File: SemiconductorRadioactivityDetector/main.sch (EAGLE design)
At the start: 27 parts, among them IC1 4011D, J1 22-05-7028-02, J2 22-05-7028-02, J3 22-05-7028-02, Q1 IRF530

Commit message: Initial unfinished version.
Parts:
- removed 11: CCFL_INVERTER_COIL, ccfl_inverter_coil:CCFL_INVERTER_COIL
- removed C10: 2n2/4k, resistor:C-EU075-042X103
- removed C5: 100u/16V, resistor:CPOL-EU153CLV-0505
- removed C8: 220n, resistor:C-EUC0805
- removed C9: 2n2/4k, rcl:C-EU075-042X103
- removed D1, D2: GF1, diode:GF1
- removed D3: ES2D, diode:ES2D
- removed D4, D5: BAV21, diode:BAV21
- removed J1, J2, J3: 22-05-7028-02, con-molex:22-05-7028-02
- removed Q1: IRF530, transistor-power:IRF530
- removed SV1: (no value), con-lstb:MA05-1
- added C11: 100n, resistor:C-EUC1206
- added IC3: LM324N, linear:LM324N
- added POWER_SUPPLY: 22-05-7028-02, con-molex:22-05-7028-02
- added R10, R11, R12, R6, R8, R9: 2k, resistor:R-EU_M1206
- added R7: (no value), pot:TRIM_EU-B64Y
- C1: value 220n -> 100n; device resistor:C-EU025-025X050 -> resistor:C-EUC1206
- C2: device resistor:C-EUC0805 -> resistor:C-EUC1206
- C4, C6: value 100u/16V -> 100n; device rcl:CPOL-EU153CLV-0505 -> resistor:C-EUC1206
- C7: value 220n -> 100n; device resistor:C-EUC0805 -> resistor:C-EUC1206
- IC1: value 4011D -> 317T; device 40xx:4011D -> linear:317T
- R1: value 4k7 -> 240R; device resistor:R-EU_M0805 -> resistor:R-EU_M1206
- R2, R3, R4: value 2k2 -> 2k; device resistor:R-EU_M0805 -> resistor:R-EU_M1206
- R5: value 33M -> 2k; device resistor:R-EU_0207/10 -> resistor:R-EU_M1206
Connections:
- removed net N$22: IC1A.O, IC1B.I0, IC1B.I1, R3.1, R4.1
- removed net N$23: C1.2, D1.A, D2.C, R2.2
- removed net N$24: D1.C, R3.2
- removed net N$25: D2.A, R4.2
- new net N$12: C6.1, IC3D.-IN, R10.2, R11.1
- new net N$13: C6.2, IC3D.OUT, R10.1
- new net N$14: IC3D.+IN, R12.2
- new net N$8: C2.1, C3.+, IC1.VI, POWER_SUPPLY-1.S
- new net N$9: R7.E, R9.2
- net GND: now also C1.2, C11.2, C4.2, IC3P.V-, POWER_SUPPLY-2.S, R12.1, R2.1, R8.2; no longer C4.-, C5.-, C6.-, C8.2, IC1P.VSS, J1-2.S, Q1.S, SV1.1, SV1.2, SV1.3
- net N$1: now also IC1.ADJ, R1.1, R2.2; no longer IC1A.I1, R2.1
- net N$10: now also R7.A, R8.1; no longer C10.2, D5.C, J2-1.S, J2-2.S, R5.2
- net N$11: now also IC3C.-IN, R7.S; no longer 11.S2, C10.1, D4.A, J3-1.S, J3-2.S, R5.1
- net N$2: now also IC3A.-IN, R3.2, R4.2; no longer IC1A.I0, R1.2, SV1.4
- net N$3: now also IC3A.OUT, IC3B.+IN, R3.1; no longer 11.P2, D3.A, Q1.D
- net N$4: now also C1.1, R4.1; no longer IC1C.O, IC1D.O, Q1.G
- net N$5: now also IC3B.-IN, R5.2, R6.2; no longer C1.1, IC1B.O, IC1C.I0, IC1C.I1, IC1D.I0, IC1D.I1
- net N$6: now also IC3B.OUT, IC3C.+IN, R11.2, R5.1; no longer 11.S1, C9.1
- net N$7: now also C4.1, R6.1; no longer C9.2, D4.C, D5.A
- net VCC: now also C11.1, IC1.VO, IC3P.V+, R1.2, R9.1; no longer 11.P1, C2.1, C3.+, C4.+, C5.+, C6.+, C8.1, D3.C, IC1P.VDD, J1-1.S, R1.1, SV1.5
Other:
- moved on the sheet: C1, C2, C3, C7, R1, R2, R3, R4, R5

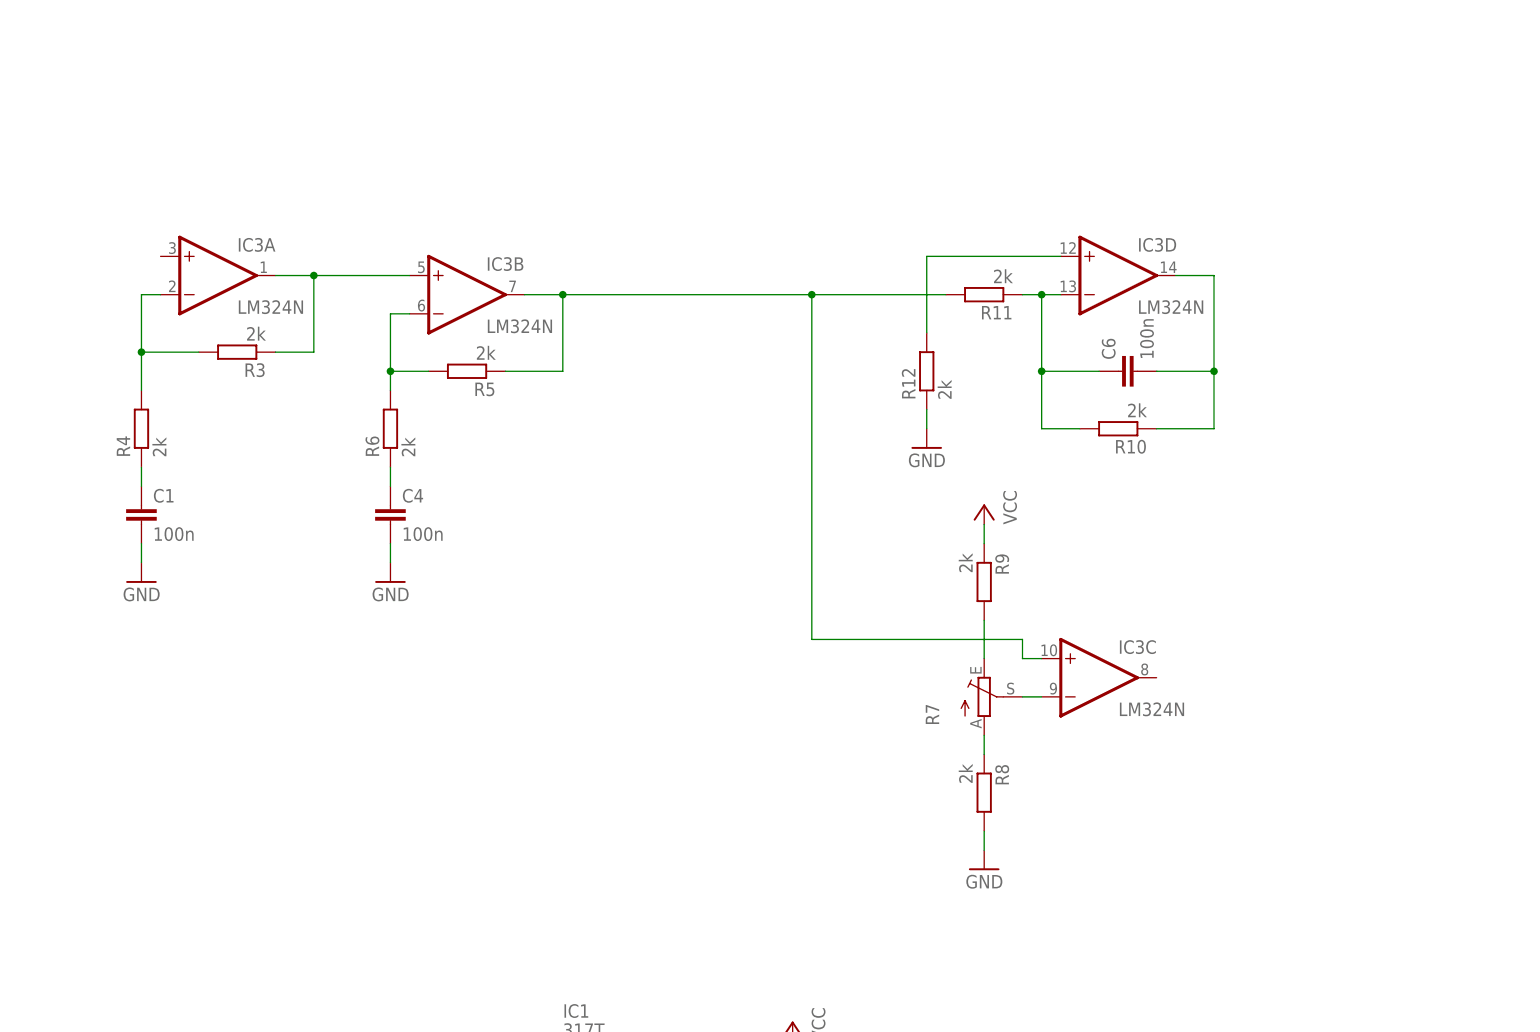
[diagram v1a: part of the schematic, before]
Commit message: Initial version,  PCB not done.
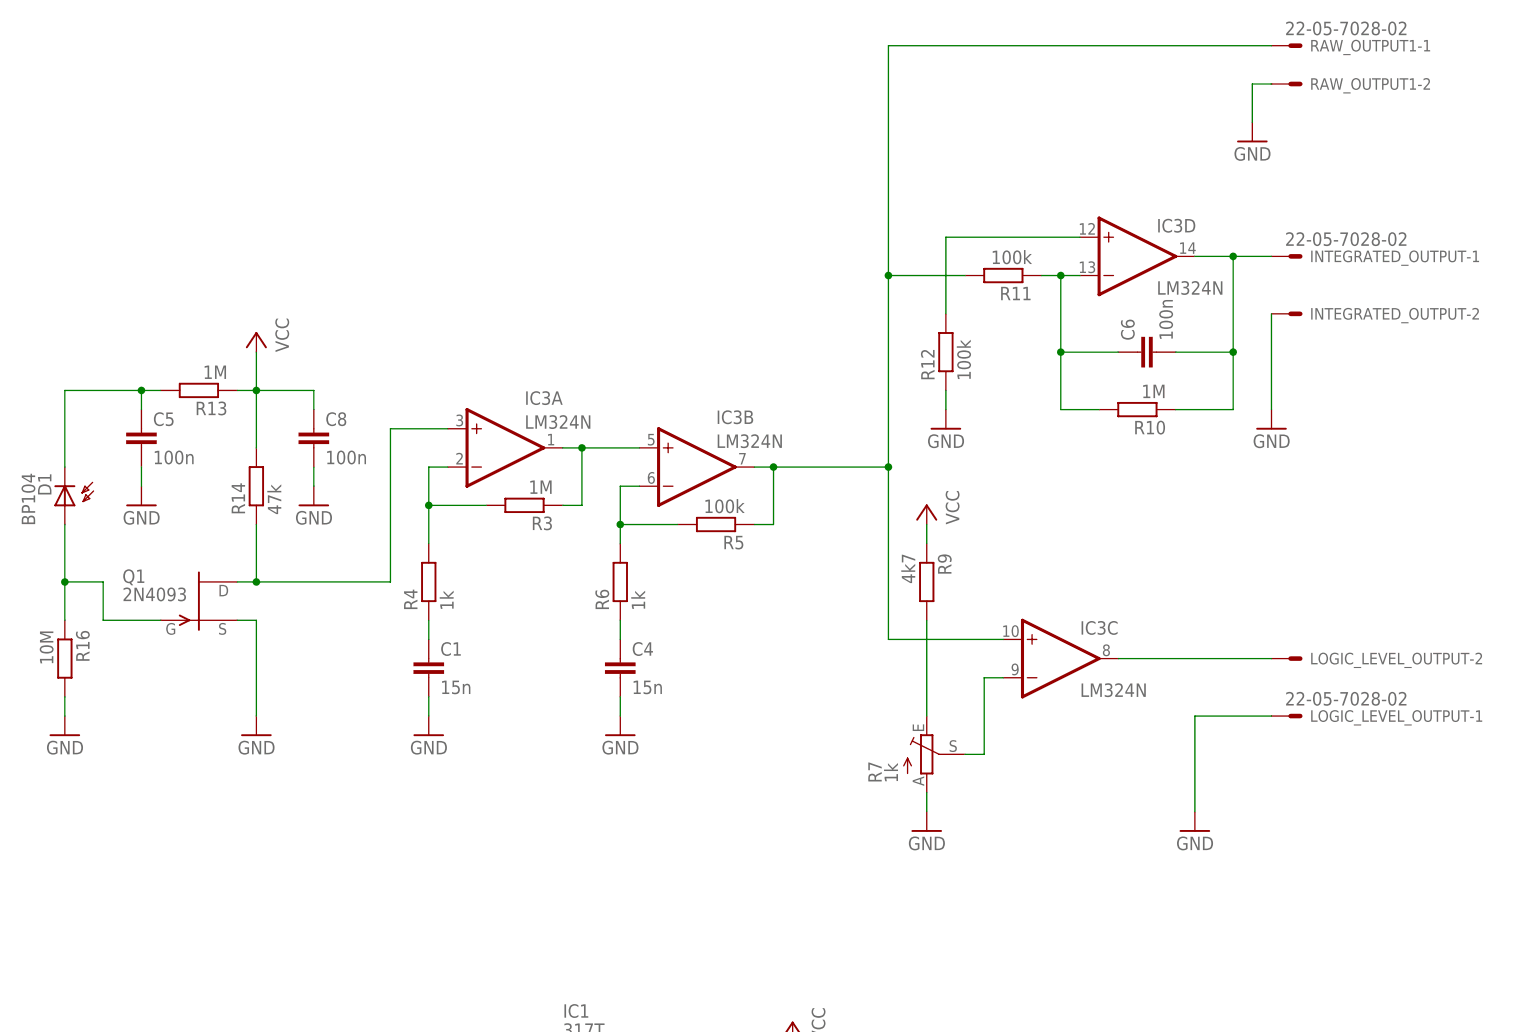
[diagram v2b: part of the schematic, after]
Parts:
- removed R8: 2k, resistor:R-EU_M1206
- added C5, C8: 100n, resistor:C-EUC1206
- added D1: BP104, opto-trans-siemens:BP104
- added INTEGRATED_OUTPUT, LOGIC_LEVEL_OUTPUT, RAW_OUTPUT1: 22-05-7028-02, con-molex:22-05-7028-02
- added Q1: 2N4093, transistor-fet:2N4093
- added R13: 1M, resistor:R-EU_M1206
- added R14: 47k, resistor:R-EU_M1206
- added R16: 10M, resistor:R-EU_0204/2V
- C1, C4: value 100n -> 15n
- R10, R3: value 2k -> 1M
- R11, R12, R5: value 2k -> 100k
- R4, R6: value 2k -> 1k
- R7: value (none) -> 1k
- R9: value 2k -> 4k7
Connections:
- removed net N$10: R7.A, R8.1
- removed net N$6: IC3B.OUT, IC3C.+IN, R11.2, R5.1
- new net N$15: IC3C.OUT, LOGIC_LEVEL_OUTPUT-2.S
- new net N$16: C5.1, D1.C, R13.2
- new net N$17: D1.A, Q1.G, R16.1
- new net N$18: IC3A.+IN, Q1.D, R14.1
- new net N$19: IC3B.OUT, IC3C.+IN, R11.2, R5.1, RAW_OUTPUT1-1.S
- net GND: now also C5.2, C8.2, INTEGRATED_OUTPUT-2.S, LOGIC_LEVEL_OUTPUT-1.S, Q1.S, R16.2, R7.A, RAW_OUTPUT1-2.S; no longer R8.2
- net N$13: now also INTEGRATED_OUTPUT-1.S
- net VCC: now also C8.1, R13.1, R14.2
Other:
- note added: "Power supply."
- moved on the sheet: C1, C4, C6, IC3A, IC3B, IC3C, IC3D, R10, R11, R12, R3, R4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

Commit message: Power supply done.
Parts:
- added C9: 100n, resistor:C-EUC1206
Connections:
- net N$12: now also C9.1
- net N$13: now also C9.2
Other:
- moved on the sheet: R10
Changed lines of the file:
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@@
 <part name="GND12" library="supply1" deviceset="GND" device=""/>
 <part name="GND13" library="supply1" deviceset="GND" device=""/>
+<part name="C9" library="resistor" deviceset="C-EU" device="C1206" value="100n"/>
 </parts>
 <sheets>
@@
 <instance part="P+1" gate="VCC" x="119.38" y="111.76" rot="MR0"/>
 <instance part="C6" gate="G$1" x="147.32" y="132.08" rot="R90"/>
-<instance part="R10" gate="G$1" x="147.32" y="124.46" rot="R180"/>
+<instance part="R10" gate="G$1" x="147.32" y="116.84" rot="R180"/>
 <instance part="R11" gate="G$1" x="129.54" y="142.24" rot="R180"/>
 <instance part="R12" gate="G$1" x="121.92" y="132.08" rot="R90"/>
@@
 <instance part="GND12" gate="1" x="5.08" y="81.28" rot="MR0"/>
 <instance part="GND13" gate="1" x="38.1" y="111.76" rot="MR0"/>
+<instance part="C9" gate="G$1" x="147.32" y="124.46" rot="R90"/>
 </instances>
 <busses>
@@
 <wire x1="137.16" y1="142.24" x2="139.7" y2="142.24" width="0.1524" layer="91"/>
 <pinref part="R10" gate="G$1" pin="2"/>
-<wire x1="142.24" y1="124.46" x2="137.16" y2="124.46" width="0.1524" layer="91"/>
-<wire x1="137.16" y1="124.46" x2="137.16" y2="132.08" width="0.1524" layer="91"/>
+<wire x1="142.24" y1="116.84" x2="137.16" y2="116.84" width="0.1524" layer="91"/>
+<wire x1="137.16" y1="116.84" x2="137.16" y2="124.46" width="0.1524" layer="91"/>
 <junction x="137.16" y="132.08"/>
 <pinref part="R11" gate="G$1" pin="1"/>
+<wire x1="137.16" y1="124.46" x2="137.16" y2="132.08" width="0.1524" layer="91"/>
 <wire x1="137.16" y1="142.24" x2="134.62" y2="142.24" width="0.1524" layer="91"/>
 <junction x="137.16" y="142.24"/>
+<pinref part="C9" gate="G$1" pin="1"/>
+<wire x1="144.78" y1="124.46" x2="137.16" y2="124.46" width="0.1524" layer="91"/>
+<junction x="137.16" y="124.46"/>
 </segment>
 </net>
@@
 <wire x1="160.02" y1="144.78" x2="154.94" y2="144.78" width="0.1524" layer="91"/>
 <pinref part="R10" gate="G$1" pin="1"/>
-<wire x1="152.4" y1="124.46" x2="160.02" y2="124.46" width="0.1524" layer="91"/>
-<wire x1="160.02" y1="124.46" x2="160.02" y2="132.08" width="0.1524" layer="91"/>
+<wire x1="152.4" y1="116.84" x2="160.02" y2="116.84" width="0.1524" layer="91"/>
+<wire x1="160.02" y1="116.84" x2="160.02" y2="124.46" width="0.1524" layer="91"/>
 <junction x="160.02" y="132.08"/>
 <pinref part="INTEGRATED_OUTPUT" gate="-1" pin="S"/>
+<wire x1="160.02" y1="124.46" x2="160.02" y2="132.08" width="0.1524" layer="91"/>
 <wire x1="160.02" y1="144.78" x2="165.1" y2="144.78" width="0.1524" layer="91"/>
 <junction x="160.02" y="144.78"/>
-</segment>
-</net>
+<pinref part="C9" gate="G$1" pin="2"/>
+<wire x1="152.4" y1="124.46" x2="160.02" y2="124.46" width="0.1524" layer="91"/>
+<junction x="160.02" y="124.46"/>
+</segment>
+</net>

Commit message: PCB done.
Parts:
- removed C11: 100n, resistor:C-EUC1206
- removed IC3: LM324N, linear:LM324N
- removed INTEGRATED_OUTPUT, LOGIC_LEVEL_OUTPUT, RAW_OUTPUT1: 22-05-7028-02, con-molex:22-05-7028-02
- removed R16: 10M, resistor:R-EU_0204/2V
- added C10: 100n, resistor:C-EUC1206
- added IC2: 317T, linear:317T
- added J2, J3, J4: 22-23-2021, con-molex:22-23-2021
- added R8: 240R, resistor:R-EU_M1206
- C1: value 15n -> 100n
- C6: value 100n -> 15n
- IC1: value 317T -> LM324N; device linear:317T -> linear:LM324N
- R1: value 240R -> 10M; device resistor:R-EU_M1206 -> resistor:R-EU_0204/2V
- R10: value 1M -> 4k7
- R11: value 100k -> 1k; device resistor:R-EU_M1206 -> pot:TRIM_EU-B64Y
- R12: device resistor:R-EU_M1206 -> resistor:R-EU_R1206
- R13: value 1M -> 100k
- R14: value 47k -> 1M
- R2: value 2k -> 1M
- R3: value 1M -> 47k
- R5: value 100k -> 1M
- R7: value 1k -> 100k; device pot:TRIM_EU-B64Y -> resistor:R-EU_M1206
- R9: value 4k7 -> 2k
- renumbered POWER_SUPPLY to J1
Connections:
- net GND: now also C6.2, IC1P.V-, J2-2.S, J3-2.S, J4-1.S, R1.2, R11.A, R9.1; no longer C11.2, IC3P.V-, INTEGRATED_OUTPUT-2.S, LOGIC_LEVEL_OUTPUT-1.S, R16.2, R2.1, R7.A, RAW_OUTPUT1-2.S
- net N$1: now also IC2.ADJ, R8.1, R9.2; no longer IC1.ADJ, R1.1, R2.2
- net N$11: now also IC1C.-IN, R11.S; no longer IC3C.-IN, R7.S
- net N$12: now also C10.1, IC1D.-IN, R13.1, R14.2; no longer C6.1, IC3D.-IN, R10.2, R11.1
- net N$13: now also C10.2, IC1D.OUT, J3-1.S, R14.1; no longer C6.2, IC3D.OUT, INTEGRATED_OUTPUT-1.S, R10.1
- net N$14: now also IC1D.+IN; no longer IC3D.+IN
- net N$15: now also IC1C.OUT, J4-2.S; no longer IC3C.OUT, LOGIC_LEVEL_OUTPUT-2.S
- net N$16: now also C1.1, R2.2; no longer C5.1, R13.2
- net N$17: now also R1.1; no longer R16.1
- net N$18: now also IC1A.+IN, R3.1; no longer IC3A.+IN, R14.1
- net N$19: now also IC1B.OUT, IC1C.+IN, J2-1.S, R13.2, R7.1; no longer IC3B.OUT, IC3C.+IN, R11.2, R5.1, RAW_OUTPUT1-1.S
- net N$2: now also IC1A.-IN, R5.2; no longer IC3A.-IN, R3.2
- net N$3: now also IC1A.OUT, IC1B.+IN, R5.1; no longer IC3A.OUT, IC3B.+IN, R3.1
- net N$4: now also C4.1; no longer C1.1
- net N$5: now also IC1B.-IN, R7.2; no longer IC3B.-IN, R5.2
- net N$7: now also C6.1; no longer C4.1
- net N$8: now also C5.1, IC2.VI; no longer C2.1, IC1.VI
- net N$9: now also R10.2, R11.E; no longer R7.E, R9.2
- net VCC: now also C2.1, IC1P.V+, IC2.VO, R10.1, R2.1, R3.2, R8.2; no longer C11.1, IC1.VO, IC3P.V+, R1.2, R13.1, R14.2, R9.1
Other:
- moved on the sheet: C1, C2, C4, C5, C6, C7, C8, C9, R1, R10, R13, R14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

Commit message: Second version. Not working.
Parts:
- removed J2, J3, J4: 22-23-2021, con-molex:22-23-2021
- removed R14: 1M, resistor:R-EU_M1206
- added C11: 10n, resistor:C-EUC0805
- added C12: 10n, rcl:C-EUC0805
- added C13: 100n, rcl:C-EUC0805
- added C14, C15: 100p, resistor:C-EUC0805
- added C16: 100n, resistor:C-EUC0805
- added IC3: OPA2333D, linear:OPA2333D
- added PAD1, PAD2: (no value), wirepad:1,6/0,8
- added TP1, TP2, TP3, TP5: PTR1TP12R, testpad:PTR1TP12R
- C1, C5, C8: device resistor:C-EUC1206 -> rcl:C-EUC0805
- C10: value 100n -> 4p7; device resistor:C-EUC1206 -> resistor:C-EUC0805
- C2: value 100n -> 330n; device resistor:C-EUC1206 -> rcl:C-EUC0805
- C4: value 15n -> 330n; device resistor:C-EUC1206 -> rcl:C-EUC0805
- C6: value 15n -> 10n; device resistor:C-EUC1206 -> resistor:C-EUC0805
- C7: value 100n -> 10n; device resistor:C-EUC1206 -> resistor:C-EUC0805
- C9: value 100n -> 100p; device resistor:C-EUC1206 -> resistor:C-EUC0805
- IC1: value LM324N -> 78L08Z; device linear:LM324N -> linear:78L08Z
- IC2: value 317T -> OPA2333D; device linear:317T -> linear:OPA2333D
- R10: value 4k7 -> 1k; device resistor:R-EU_M1206 -> rcl:R-EU_R0805
- R11: device pot:TRIM_EU-B64Y -> rcl:R-EU_R0805
- R12: value 100k -> 10k; device resistor:R-EU_R1206 -> rcl:R-EU_R0805
- R13: value 100k -> 10k; device resistor:R-EU_M1206 -> rcl:R-EU_R0805
- R2: value 1M -> 10k; device resistor:R-EU_M1206 -> rcl:R-EU_R0805
- R3: value 47k -> 10k; device resistor:R-EU_M1206 -> rcl:R-EU_R0805
- R4: value 1k -> 470k; device resistor:R-EU_M1206 -> rcl:R-EU_R0805
- R5: value 1M -> 39k; device resistor:R-EU_M1206 -> rcl:R-EU_R0805
- R6: value 1k -> 10R; device resistor:R-EU_M1206 -> rcl:R-EU_R0805
- R7: value 100k -> 1k; device resistor:R-EU_M1206 -> rcl:R-EU_R0805
- R8: value 240R -> 10k; device resistor:R-EU_M1206 -> rcl:R-EU_R0805
- R9: value 2k -> 10M; device resistor:R-EU_M1206 -> rcl:R-EU_0204/2V
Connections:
- removed net N$1: IC2.ADJ, R8.1, R9.2
- removed net N$12: C10.1, C9.1, IC1D.-IN, R13.1, R14.2
- removed net N$18: IC1A.+IN, Q1.D, R3.1
- removed net N$19: IC1B.OUT, IC1C.+IN, J2-1.S, R13.2, R7.1
- removed net N$5: IC1B.-IN, R6.2, R7.2
- removed net VCC: C2.1, C7.1, C8.1, IC1P.V+, IC2.VO, R10.1, R2.1, R3.2, R8.2
- new net N$10: C9.1, IC2A.-IN, R7.1, R8.2
- new net N$20: C10.2, C11.1, IC3A.OUT, R9.1
- new net N$22: C12.1, C9.2, IC2A.OUT, R8.1
- new net N$6: C6.1, Q1.D, R5.1
- new net V+: C13.1, C16.1, C4.1, C8.1, IC1.VO, IC2P.V+, IC3P.V+, R2.2, R4.1, R5.2, TP3.TP
- new net V_REF: C1.1, IC2A.+IN, IC2B.+IN, IC3A.+IN, IC3B.+IN, R2.1, R3.2, TP1.TP
- net GND: now also C13.2, C16.2, IC1.GND, IC2P.V-, IC3P.V-, PAD2.P, R3.1; no longer C6.2, C7.2, IC1P.V-, J2-2.S, J3-2.S, J4-1.S, R11.A, R12.1, R9.1
- net N$11: now also C7.2, R7.2; no longer IC1C.-IN, R11.S
- net N$13: now also C14.1, IC2B.-IN, R11.1, R12.2; no longer C10.2, C9.2, IC1D.OUT, J3-1.S, R14.1
- net N$14: now also C12.2, R11.2; no longer IC1D.+IN, R12.2
- net N$15: now also C11.2, R10.2; no longer IC1C.OUT, J4-2.S
- net N$16: now also C2.1, R4.2; no longer C1.1, R2.2
- net N$2: now also C6.2, R6.2; no longer IC1A.-IN, R4.2, R5.2
- net N$3: now also C14.2, IC2B.OUT, PAD1.P, R12.1; no longer IC1A.OUT, IC1B.+IN, R5.1
- net N$4: now also C10.1, IC3A.-IN, R6.1, R9.2; no longer C4.1, R4.1
- net N$7: now also C15.2, C7.1, IC3B.OUT, R13.1, TP5.TP; no longer C6.1, R6.1
- net N$8: now also IC1.VI, TP2.TP; no longer IC2.VI
- net N$9: now also C15.1, IC3B.-IN, R10.1, R13.2; no longer R10.2, R11.E
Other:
- moved on the sheet: C1, C10, C2, C3, C4, C5, C6, C7, C8, C9, D1, J1-1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
